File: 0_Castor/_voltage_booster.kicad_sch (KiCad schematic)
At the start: 10 parts, among them U2 TLV61070ADBV, U3 TXU0101DBV

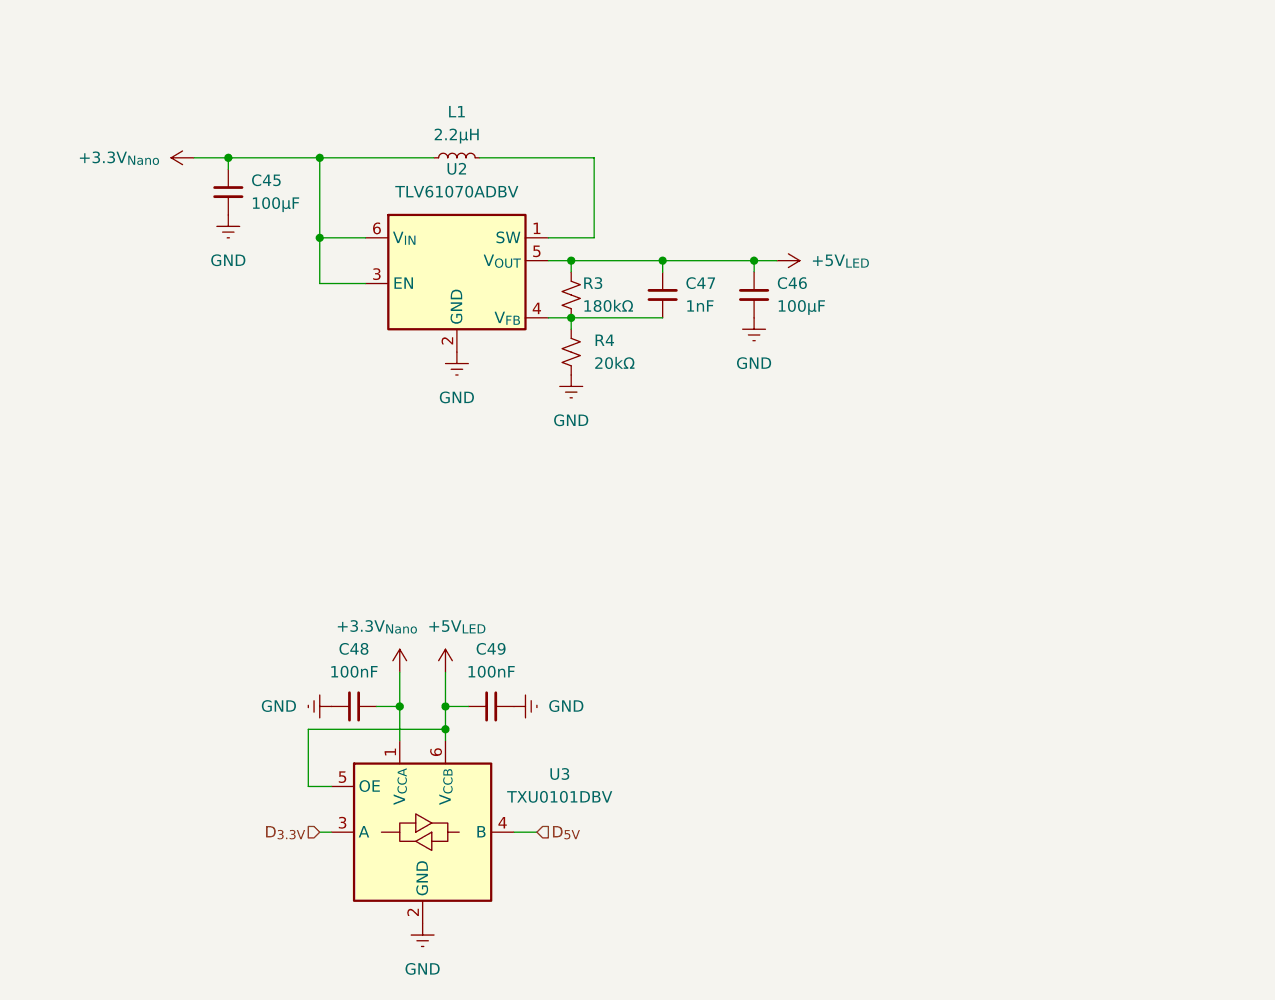
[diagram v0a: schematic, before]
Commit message: feat: add voltage booster for LEDs power supply
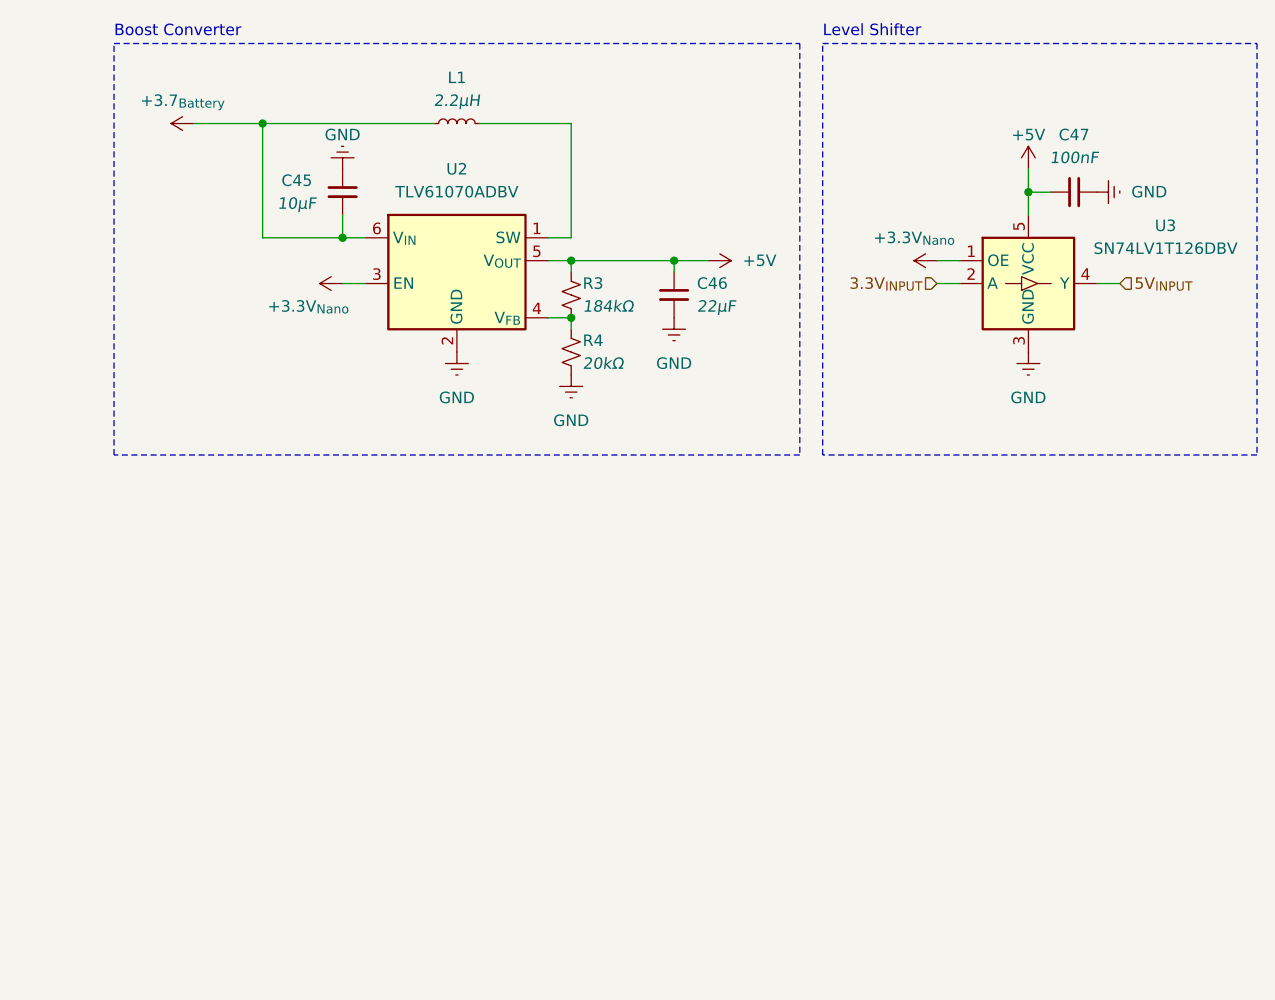
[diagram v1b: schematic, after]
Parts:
- removed C48, C49: 100nF, Capacitor_SMD:C_0603_1608Metric, symbol Device:C_Small
- removed U3: TXU0101DBV, Package_TO_SOT_SMD:SOT-23-6, symbol Logic_LevelTranslator:TXB0101DBV
- added U3: SN74LV1T126DBV, Package_TO_SOT_SMD:SOT-23-5, symbol Logic_LevelTranslator:SN74LV1T125DBV
- C45: value 100µF -> 10µF
- C46: value 100µF -> 22µF
- C47: value 1nF -> 100nF
- R3: value 180kΩ -> 184kΩ
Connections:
- net +3.3V_{Nano}: now also U3.1 (OE); no longer C45.1, L1.1, U2.6 (V_{IN})
- net GND: now also C47.1, U3.3 (GND)
- net at R3.2, R4.1, U2.4 (V_{FB}): no longer C47.2
- net +5V_{LED} renamed +5V
- net +5V: now also C47.2, U3.5 (VCC); no longer C47.1
- new net +3.7_{Battery}: C45.1, L1.1, U2.6 (V_{IN})
- new net 3.3V_{INPUT}: U3.2 (A)
- new net 5V_{INPUT}: U3.4 (Y)
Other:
- note added: "Boost Converter"
- note added: "Level Shifter"
- moved on the sheet: C45, C46, L1
